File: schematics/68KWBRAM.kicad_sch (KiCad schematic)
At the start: 8 parts, among them U1 68000

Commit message: WIP
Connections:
- net VCC: no longer 6M.28 (VCC), 7M.28 (VCC)
- new net BAT_VCC: 6M.28 (VCC), 7M.28 (VCC)
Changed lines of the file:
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@@
   (junction (at 256.54 83.82) (diameter 0) (color 0 0 0 0)
   )
-  (junction (at 372.11 33.02) (diameter 0) (color 0 0 0 0)
+  (junction (at 372.11 30.48) (diameter 0) (color 0 0 0 0)
   )
   (junction (at 311.15 137.16) (diameter 0) (color 0 0 0 0)
@@
     (stroke (width 0) (type default))
   )
+  (wire (pts (xy 339.09 30.48) (xy 372.11 30.48))
+    (stroke (width 0) (type default))
+  )
   (wire (pts (xy 237.49 113.03) (xy 243.84 113.03))
     (stroke (width 0) (type default))
@@
     (stroke (width 0) (type default))
   )
+  (wire (pts (xy 339.09 35.56) (xy 339.09 30.48))
+    (stroke (width 0) (type default))
+  )
   (wire (pts (xy 114.3 57.15) (xy 128.27 57.15))
     (stroke (width 0) (type default))
@@
     (stroke (width 0) (type default))
   )
+  (wire (pts (xy 377.19 30.48) (xy 372.11 30.48))
+    (stroke (width 0) (type default))
+  )
   (bus (pts (xy 317.5 102.87) (xy 317.5 105.41))
     (stroke (width 0) (type default))
@@
     (stroke (width 0) (type default))
   )
-  (wire (pts (xy 339.09 33.02) (xy 372.11 33.02))
-    (stroke (width 0) (type default))
-  )
   (bus (pts (xy 148.59 41.91) (xy 148.59 39.37))
     (stroke (width 0) (type default))
@@
     (stroke (width 0) (type default))
   )
-  (wire (pts (xy 372.11 30.48) (xy 372.11 33.02))
+  (wire (pts (xy 372.11 30.48) (xy 372.11 87.63))
     (stroke (width 0) (type default))
   )
@@
     (stroke (width 0) (type default))
   )
-  (wire (pts (xy 339.09 33.02) (xy 339.09 35.56))
-    (stroke (width 0) (type default))
-  )
-  (wire (pts (xy 372.11 33.02) (xy 372.11 87.63))
-    (stroke (width 0) (type default))
-  )
   (bus (pts (xy 209.55 69.85) (xy 209.55 72.39))
     (stroke (width 0) (type default))
@@
     )
   )
+  (global_label "BAT_VCC" (shape input) (at 377.19 30.48 0) (fields_autoplaced)
+    (effects (font (size 1.27 1.27)) (justify left))
+    (property "Intersheetrefs" "${INTERSHEET_REFS}" (at 387.13 30.48 0)
+      (effects (font (size 1.27 1.27)) (justify left))
+    )
+  )
   (global_label "RESET" (shape input) (at 53.34 125.73 180) (fields_autoplaced)
     (effects (font (size 1.27 1.27)) (justify right))
@@
         )
       )
-    )
-  )
-  (symbol (lib_id "power:VCC") (at 372.11 30.48 0) (unit 1)
-    (in_bom yes) (on_board yes) (dnp no) (fields_autoplaced)
-    (property "Reference" "#PWR010" (at 372.11 34.29 0)
-      (effects (font (size 1.27 1.27)) hide)
-    )
-    (property "Value" "VCC" (at 372.11 26.3469 0)
-      (effects (font (size 1.27 1.27)))
-    )
-    (property "Footprint" "" (at 372.11 30.48 0)
-      (effects (font (size 1.27 1.27)) hide)
-    )
-    (property "Datasheet" "" (at 372.11 30.48 0)
-      (effects (font (size 1.27 1.27)) hide)
-    )
-    (pin "1")
-    (instances
-      (project "MVS"
-        (path "/8d0803ab-15ed-47a7-8dcb-ab27dc5b29c2"
-          (reference "#PWR010") (unit 1)
-        )
-        (path "/8d0803ab-15ed-47a7-8dcb-ab27dc5b29c2/0b42d888-4b79-4625-b2d5-9f4b583469ed"
-          (reference "#PWR036") (unit 1)
-        )
-      )

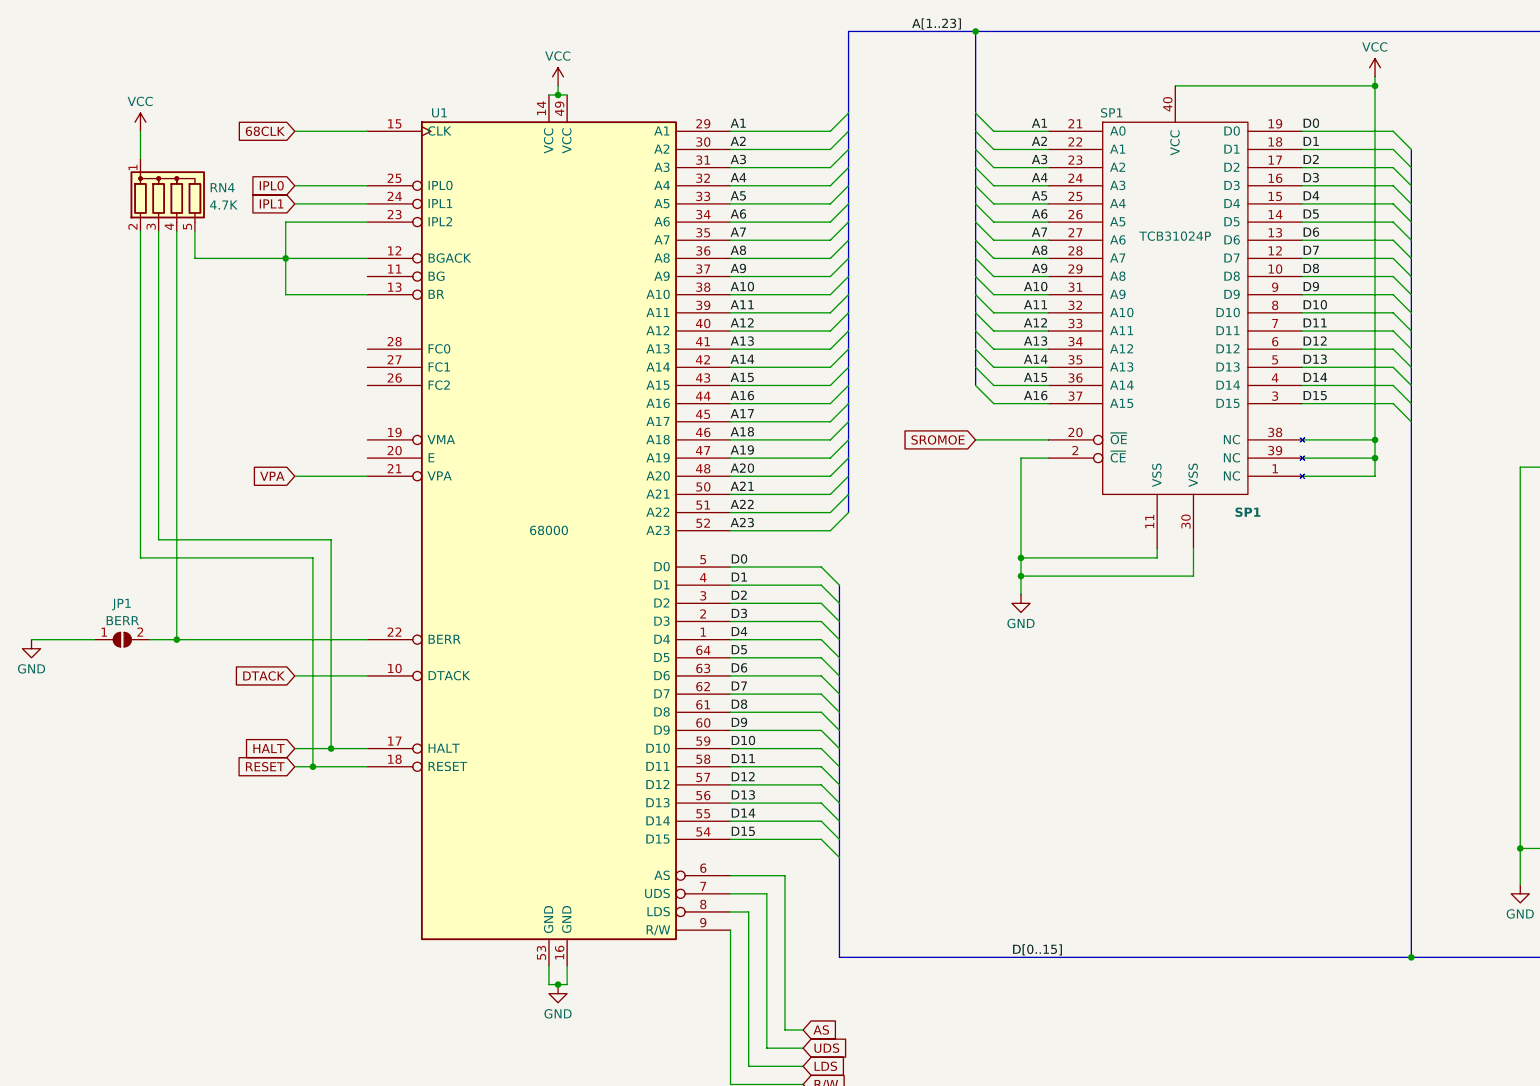
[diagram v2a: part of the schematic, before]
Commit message: update "main" schematics
Adding LSPC2-A2, NEO-B1, L0 ROM
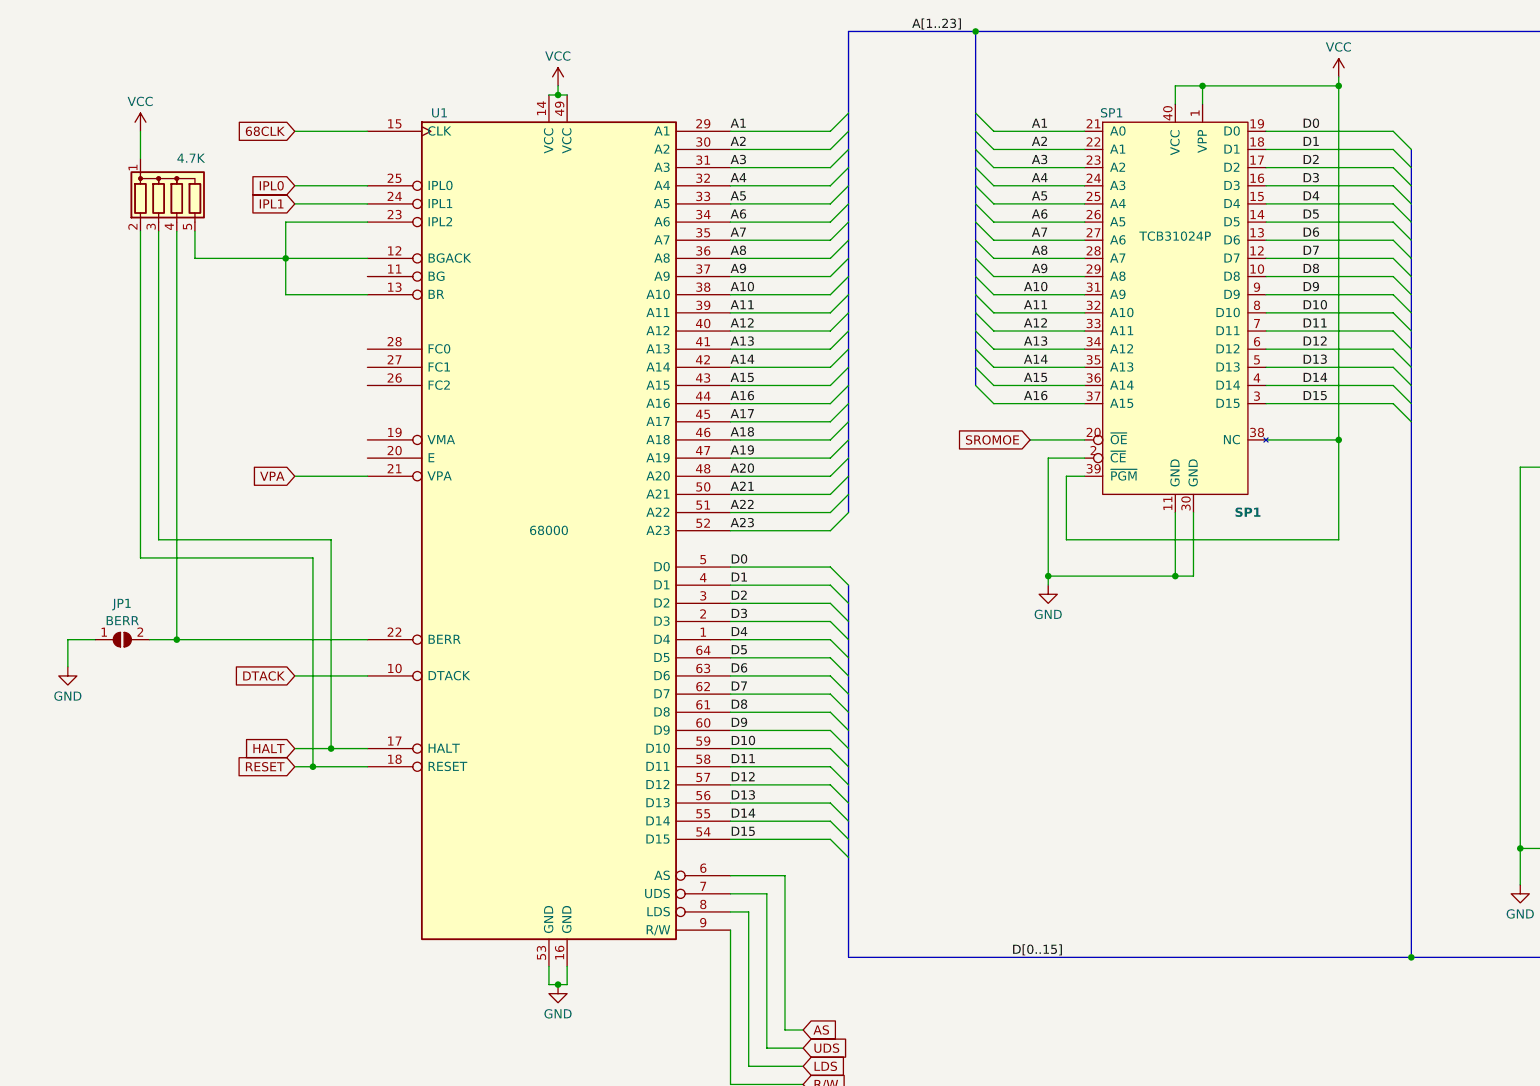
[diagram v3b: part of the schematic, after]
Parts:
- SP1: symbol cbm-steve:27C1024 -> 0-Custom-cbm-steve:27C1024
